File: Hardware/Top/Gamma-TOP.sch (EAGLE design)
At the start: 51 parts, among them SW6 SWITCH.MOM, SW7 SWITCH.MOM, U2 NRF52832_MODULE_MDBT42, U4 PCF8523

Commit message: Update to Top and Bottom Boards.  Top is not complete as of yet, and the bottom is ready for a check.  Routing not performed yet
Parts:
- removed R8, R9: 10k, LinnesLab-Passives:RESISTOR0603
- added C22: 100n, LinnesLab-Passives:CAPACITOR0603
- added C23, C24: 47p, LinnesLab-Passives:CAPACITOR0603
- added J1: (no value), LinnesLab-Connectors:CONN_07
- added JP2: (no value), LinnesLab-Switches:JUMPER-SMT_2_NO_SILK
- added LED5: RED, LinnesLab-LED:LED0603
- added LED6: YELLOW, LinnesLab-LED:LED0603
- added R1, R2: 0, LinnesLab-Passives:RESISTOR0603
- added R10, R16: 10k, LinnesLab-Passives:RESISTOR0603
- added R17, R18: 27, LinnesLab-Passives:RESISTOR0603
- added R19, R20: 1k, LinnesLab-Passives:RESISTOR0603
- added U5: FT231XS, LinnesLab-DigitalIC:FT231XS
- renumbered SW6 to SW1, SW7 to SW2
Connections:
- removed net BATT: R13.1, R14.2
- removed net CD1: SD2.CARD_DETECT
- removed net CHRG.STAT: CHRG2.STAT, R12.1
- removed net CS.OLED: U3./CS
- removed net DC.OLED: U3.DC/I2C_SA0
- removed net RESET.OLED: U3./RES
- removed net RXD: U2.P0.08
- removed net SD.CS: SD2.CS
- removed net SW1: SW1.1
- removed net SW2: SW2.1
- removed net TXD: U2.P0.06
- new net !CTS: JP2.2, U5.!CTS
- new net A4/BATT: R13.1, R14.2, U2.P0.28/AIN4
- new net A6/TIA: U2.P0.30/AIN6
- new net A7/PPG: U2.P0.31/AIN7
- new net D11/SW1: SW1.1, U2.P0.11
- new net D15/SW2: SW2.1, U2.P0.15
- new net D16/CS.OLED: U2.P0.16, U3./CS
- new net D27/CHRG.STATUS: CHRG2.STAT, R12.1, U2.P0.27
- new net D29/LED.CTRL: U2.P0.29/AIN5
- new net D3/RESET.OLED: U2.P0.03/AIN1, U3./RES
- new net D4/DC.OLED: U2.P0.04/AIN2, U3.DC/I2C_SA0
- new net D5/CD1: SD2.CARD_DETECT, U2.P0.05/AIN3
- new net D7/SD.CS: SD2.CS, U2.P0.07
- new net FT3V3: U5.3V3OUT
- new net N$23: R17.2, U5.USBDM
- new net N$24: R18.2, U5.USBDP
- new net N$25: LED5.C, R19.2
- new net N$26: LED6.C, R20.2
- new net RXD.FT: R2.1, U5.RXD
- new net RXD.NRF: R1.2, U2.P0.08
- new net RXLED: R19.1, U5.CBUS1
- new net TXD.FT: R1.1, U5.TXD
- new net TXD.NRF: R2.2, U2.P0.06
- new net TXLED: R20.1, U5.CBUS2
- net 3.3V: now also C22.2, LED5.A, LED6.A, R10.1, R16.1, U5.!RESET, U5.VCCIO; no longer R8.2, R9.2
- net DTR: now also U5.!DTR
- net GND: now also C22.1, C23.2, C24.1, JP2.1, U5.GND@16, U5.GND@6
- net SCL: now also R10.2; no longer R8.1
- net SDA: now also R16.2; no longer R9.1
- net USB+: now also C23.1, R18.1
- net USB-: now also C24.2, R17.1
- net V_USB: now also U5.VCC
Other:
- note added: "I don't remember if CTS needs to be grounded or left floating so here's a jumper to ground so it can be configued either way dynamically."
- note added: "TXD goes to RX on the other device RXD goes to TX on the other device"
- note added: "USB Serial"

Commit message: Finished Take 004 up until deletion of NFC capacitors.  Board partially routed
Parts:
- removed C22: 100n, LinnesLab-Passives:CAPACITOR0603
- removed C23, C24: 47p, LinnesLab-Passives:CAPACITOR0603
- removed CHRG2: MCP73831, LinnesLab-Power:MCP73831
- removed CORTEX1: CORTEX_DEBUG_PTH, LinnesLab-Connectors:CORTEX_DEBUG_PTH
- removed D4, D5: (no value), LinnesLab-DiscreteSemi:SCHOTTKY-USC
- removed JP2: (no value), LinnesLab-Switches:JUMPER-SMT_2_NO_SILK
- removed LDO2: MIC5504, LinnesLab-Power:MIC5504
- removed LED5: RED, LinnesLab-LED:LED0603
- removed LED6: YELLOW, LinnesLab-LED:LED0603
- removed R19, R20: 1k, LinnesLab-Passives:RESISTOR0603
- removed SD2: (no value), LinnesLab-Connectors:MICROSD
- removed U5: FT231XS, LinnesLab-DigitalIC:FT231XS
- removed USB2: USB.MICRO-BIGGERPADS, LinnesLab-Connectors:USB.MICRO-BIGGERPADS
- removed XTAL3: 32.7680kHz, LinnesLab-Clocks:CRYSTALECS-.327-12.5-12-C-TR
- added C1: 47p, LinnesLab-Passives:CAPACITOR0603
- added C3: 100n, LinnesLab-Passives:CAPACITOR0603
- added C4: 4.7u, LinnesLab-Passives:CAPACITOR0603
- added CHRG1: MCP73831, LinnesLab-Power:MCP73831
- added D2, D3: (no value), LinnesLab-DiscreteSemi:SCHOTTKY-USC
- added DEBUG1: CORTEX_DEBUG_PTH, LinnesLab-Connectors:CORTEX_DEBUG_PTH
- added JP1: (no value), LinnesLab-Switches:JUMPER-SMT_2_NO_SILK
- added LDO1: MIC5504, LinnesLab-Power:MIC5504
- added LED1: RED, LinnesLab-LED:LED0603
- added LED2: YELLOW, LinnesLab-LED:LED0603
- added R8: (no value), LinnesLab-Passives:RESISTOR0603
- added R9: 100k, LinnesLab-Passives:RESISTOR0603
- added SD1: (no value), LinnesLab-Connectors:MICROSD
- added U1: FT231XS, LinnesLab-DigitalIC:FT231XS
- added USB1: USB.MICRO-BIGGERPADS, LinnesLab-Connectors:USB.MICRO-BIGGERPADS
- added XTAL1: 32.768kHz, LinnesLab-Clocks:CRYSTALECS-.327-12.5-12-C-TR
- C10, C11: value 300p -> 2.2uF; device LinnesLab-Passives:CAPACITOR0603 -> LinnesLab-Passives:CAPACITOR0402
- C12: value 10u -> 1u; device LinnesLab-Passives:CAPACITOR0805 -> LinnesLab-Passives:CAPACITOR0603
- C13: value 2.2uF -> 4.7u; device LinnesLab-Passives:CAPACITOR0402 -> LinnesLab-Passives:CAPACITOR0603
- C14: value 100n -> 1u
- C15: value 2.2uF -> 10u; device LinnesLab-Passives:CAPACITOR0402 -> LinnesLab-Passives:CAPACITOR0805
- C16: value 10uF -> (none)
- C17: value 2.2uF -> (none); device LinnesLab-Passives:CAPACITOR0402 -> LinnesLab-Passives:CAPACITOR0603
- C18, C19: value 2.2uF -> 300p; device LinnesLab-Passives:CAPACITOR0402 -> LinnesLab-Passives:CAPACITOR0603
- C2: value 1u -> 47p
- C20: value 4.7u -> 100n
- C21: value 4.7u -> 1u
- C6: value 1u -> 10uF
- C7: value 1u -> 2.2uF; device LinnesLab-Passives:CAPACITOR0603 -> LinnesLab-Passives:CAPACITOR0402
- C8, C9: value (none) -> 2.2uF; device LinnesLab-Passives:CAPACITOR0603 -> LinnesLab-Passives:CAPACITOR0402
- J1: device LinnesLab-Connectors:CONN_07 -> LinnesLab-Connectors:CONN_07-1.27MM
- R1, R2: value 0 -> 27
- R10: value 10k -> 100k
- R11: value (none) -> 100k
- R12, R13: value 100k -> 0
- R14, R15: value 100k -> 10k
- R16, R5, R6: value 10k -> 1k
- R17: value 27 -> 1k
- R18: value 27 -> 10k
- R3: value 1k -> 100k
- R4: value 1k -> 10k
- U2: value NRF52832_MODULE_MDBT42 -> (none); device LinnesLab-Microcontrollers:NRF52832_MODULE_MDBT42 -> LinnesLab-Displays:DISP_OLED_UG-2864HSWEG01-NO-WRAPAROUND
- U3: value (none) -> NRF52832_MODULE_MDBT42; device LinnesLab-Displays:DISP_OLED_UG-2864HSWEG01-NO-WRAPAROUND -> LinnesLab-Microcontrollers:NRF52832_MODULE_MDBT42
- XTAL2: value 32.768kHz -> 32.7680kHz; FREQ (none) -> 32.7680KHZ
- renumbered L2 to L1
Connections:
- net !CTS: now also JP1.2, U1.!CTS; no longer JP2.2, U5.!CTS
- net 3.3V: now also C10.2, C11.2, C12.1, C15.2, C21.1, C3.2, D3.C, DEBUG1.VCC, J1.4, LDO1.OUT, LED1.A, LED2.A, R14.1, R15.1, R18.2, R9.2, SD1.VDD, U1.!RESET, U1.VCCIO, U2.VBAT; no longer C12.2, C17.2, C19.2, C2.1, C22.2, C6.1, CORTEX1.VCC, D1.C, LDO2.OUT, LED5.A, LED6.A, R10.1, R15.2, R16.1, R5.2, SD2.VDD, U3.VBAT, U5.!RESET, U5.VCCIO
- net A4/BATT: now also R10.1, R11.2, U3.P0.28/AIN4; no longer R13.1, R14.2, U2.P0.28/AIN4
- net A6/TIA: now also J1.6, U3.P0.30/AIN6; no longer U2.P0.30/AIN6
- net A7/PPG: now also J1.7, U3.P0.31/AIN7; no longer U2.P0.31/AIN7
- net CD2: now also SD1.CARD_DETECT1; no longer SD2.CARD_DETECT1
- net D11/SW1: now also U3.P0.11; no longer U2.P0.11
- net D15/SW2: now also U3.P0.15; no longer U2.P0.15
- net D16/CS.OLED: now also U2./CS, U3.P0.16; no longer U2.P0.16, U3./CS
- net D27/CHRG.STATUS: now also CHRG1.STAT, R3.1, U3.P0.27; no longer CHRG2.STAT, R12.1, U2.P0.27
- net D29/LED.CTRL: now also J1.5, U3.P0.29/AIN5; no longer U2.P0.29/AIN5
- net D3/RESET.OLED: now also U2./RES, U3.P0.03/AIN1; no longer U2.P0.03/AIN1, U3./RES
- net D4/DC.OLED: now also U2.DC/I2C_SA0, U3.P0.04/AIN2; no longer U2.P0.04/AIN2, U3.DC/I2C_SA0
- net D5/CD1: now also SD1.CARD_DETECT, U3.P0.05/AIN3; no longer SD2.CARD_DETECT, U2.P0.05/AIN3
- net D7/SD.CS: now also SD1.CS, U3.P0.07; no longer SD2.CS, U2.P0.07
- net DFU: now also SW4.B, U3.P0.20; no longer SW3.B, U2.P0.20
- net DTR: now also C20.1, U1.!DTR; no longer C14.1, U5.!DTR
- net FRST: now also U3.P0.22; no longer U2.P0.22
- net FT3V3: now also U1.3V3OUT; no longer U5.3V3OUT
- net GND: now also C1.1, C10.1, C11.1, C12.2, C13.2, C14.2, C15.1, C17.2, C18.2, C19.2, C21.2, C3.1, C4.1, C6.1, CHRG1.VSS, DEBUG1.GND@3, DEBUG1.GND@5, DEBUG1.GNDDTCT, DEBUG1.KEY, J1.3, JP1.1, LDO1.GND, R4.1, R8.1, R9.1, SD1.GND, SD1.GND1, SD1.VSS, SW3.B, SW4.A, U1.GND@16, U1.GND@6, U2.BS0, U2.BS2, U2.NC(GND)@1, U2.NC(GND)@2, U2.VLSS, U2.VSS, U3.GND@1, U3.GND@2, U3.GND@3, U3.GND@4, USB1.GND; no longer C10.2, C11.2, C12.1, C17.1, C18.1, C19.1, C20.2, C21.1, C22.1, C23.2, C24.1, C6.2, C7.2, C9.2, CHRG2.VSS, CORTEX1.GND@3, CORTEX1.GND@5, CORTEX1.GNDDTCT, CORTEX1.KEY, JP2.1, LDO2.GND, R14.1, R15.1, R6.1, SD2.GND, SD2.GND1, SD2.VSS, SW3.A, SW4.B, U2.GND@1, U2.GND@2, U2.GND@3, U2.GND@4, U3.BS0, U3.BS2, U3.NC(GND)@1, U3.NC(GND)@2, U3.VLSS, U3.VSS, U5.GND@16, U5.GND@6, USB2.GND
- net LED1: now also R16.2, U3.P0.17; no longer R3.2, U2.P0.17
- net LED2: now also R17.2, U3.P0.19; no longer R4.2, U2.P0.19
- net MISO: now also SD1.DATA_OUT, U3.P0.14; no longer SD2.DATA_OUT, U2.P0.14
- net MOSI: now also SD1.DATA_IN, U2.D1/SPI_SDIN/I2C_SDA, U3.P0.13; no longer SD2.DATA_IN, U2.P0.13, U3.D1/SPI_SDIN/I2C_SDA
- net N$1: now also R4.2, U2.BS1; no longer R6.2, U3.BS1
- net N$10: now also R17.1; no longer R4.1
- net N$11: now also U3.DCC; no longer U2.DCC
- net N$12: now also C14.1, U3.DEC4; no longer C7.1, U2.DEC4
- net N$13: now also C6.2, U2.VCC; no longer C16.2, U3.VCC
- net N$14: now also DEBUG1.NC/TDI; no longer CORTEX1.NC/TDI
- net N$15: now also C8.2, U2.VCOMH; no longer C18.2, U3.VCOMH
- net N$17: now also CHRG1.PROG, R8.2; no longer CHRG2.PROG, R11.2
- net N$19: now also XTAL2.1; no longer XTAL3.1
- net N$2: now also U2.IREF; no longer U3.IREF
- net N$20: now also XTAL2.2; no longer XTAL3.2
- net N$23: now also R1.2, U1.USBDM; no longer R17.2, U5.USBDM
- net N$24: now also R2.2, U1.USBDP; no longer R18.2, U5.USBDP
- net N$25: now also LED1.C, R5.2; no longer LED5.C, R19.2
- net N$26: now also LED2.C, R6.2; no longer LED6.C, R20.2
- net N$3: now also C9.2, U2.C2P; no longer C13.2, U3.C2P
- net N$4: now also C16.2, U3.P0.00/XL1, XTAL1.1; no longer C8.2, U2.P0.00/XL1, XTAL2.1
- net N$5: now also C9.1, U2.C2N; no longer C13.1, U3.C2N
- net N$6: now also C17.1, U3.P0.01/XL2, XTAL1.2; no longer C9.1, U2.P0.01/XL2, XTAL2.2
- net N$7: now also C7.2, U2.C1P; no longer C15.2, U3.C1P
- net N$8: now also C7.1, U2.C1N; no longer C15.1, U3.C1N
- net N$9: now also R16.1; no longer R3.1
- net P0.09/NFC1: now also C18.1, U3.P0.09; no longer C11.1, U2.P0.09
- net P0.10/NFC2: now also C19.1, U3.P0.10; no longer C10.1, U2.P0.10
- net RESET: now also C20.2, D3.A, DEBUG1.!RESET, R18.1, SW3.A, U3.P0.21/RESET; no longer C14.2, CORTEX1.!RESET, D1.A, R5.1, SW4.A, U2.P0.21/RESET
- net RXD.FT: now also R13.1, U1.RXD; no longer R2.1, U5.RXD
- net RXD.NRF: now also R12.2, U3.P0.08; no longer R1.2, U2.P0.08
- net RXLED: now also R5.1, U1.CBUS1; no longer R19.1, U5.CBUS1
- net SCK: now also SD1.SCLK, U2.D0/SPI_SCLK/I2C_SCK, U3.P0.12; no longer SD2.SCLK, U2.P0.12, U3.D0/SPI_SCLK/I2C_SCK
- net SCL: now also J1.2, R15.2, U3.P0.26; no longer R10.2, U2.P0.26
- net SDA: now also J1.1, R14.2, U3.P0.25; no longer R16.2, U2.P0.25
- net SWCLK: now also DEBUG1.SWDCLK/TCK, U3.SWDCLK; no longer CORTEX1.SWDCLK/TCK, U2.SWDCLK
- net SWDIO: now also DEBUG1.SWDIO/TMS, U3.SWDIO; no longer CORTEX1.SWDIO/TMS, U2.SWDIO
- net SWO: now also DEBUG1.SWO/TDO, U3.P0.18/SWO; no longer CORTEX1.SWO/TDO, U2.P0.18/SWO
- net TXD.FT: now also R12.1, U1.TXD; no longer R1.1, U5.TXD
- net TXD.NRF: now also R13.2, U3.P0.06; no longer R2.2, U2.P0.06
- net TXLED: now also R6.1, U1.CBUS2; no longer R20.1, U5.CBUS2
- net USB+: now also C2.1, R2.1, USB1.D+; no longer C23.1, R18.1, USB2.D+
- net USB-: now also C1.2, R1.1, USB1.D-; no longer C24.2, R17.1, USB2.D-
- net VIN: now also C4.2, CHRG1.VIN, D1.C, D2.C, LDO1.EN, LDO1.IN, R3.2; no longer C21.2, CHRG2.VIN, D4.C, D5.C, LDO2.EN, LDO2.IN, R12.2
- net VLIPO: now also C13.1, CHRG1.VBAT, D1.A, R10.2; no longer C20.1, CHRG2.VBAT, D4.A, R13.2
- net V_USB: now also D2.A, U1.VCC, USB1.V+; no longer D5.A, U5.VCC, USB2.V+
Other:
- note added: "Gamma Top Version A"
- note added: "Pins"
- moved on the sheet: C10, C11, C12, C13, C14, C15, C16, C17, C18, C19, C2, C20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

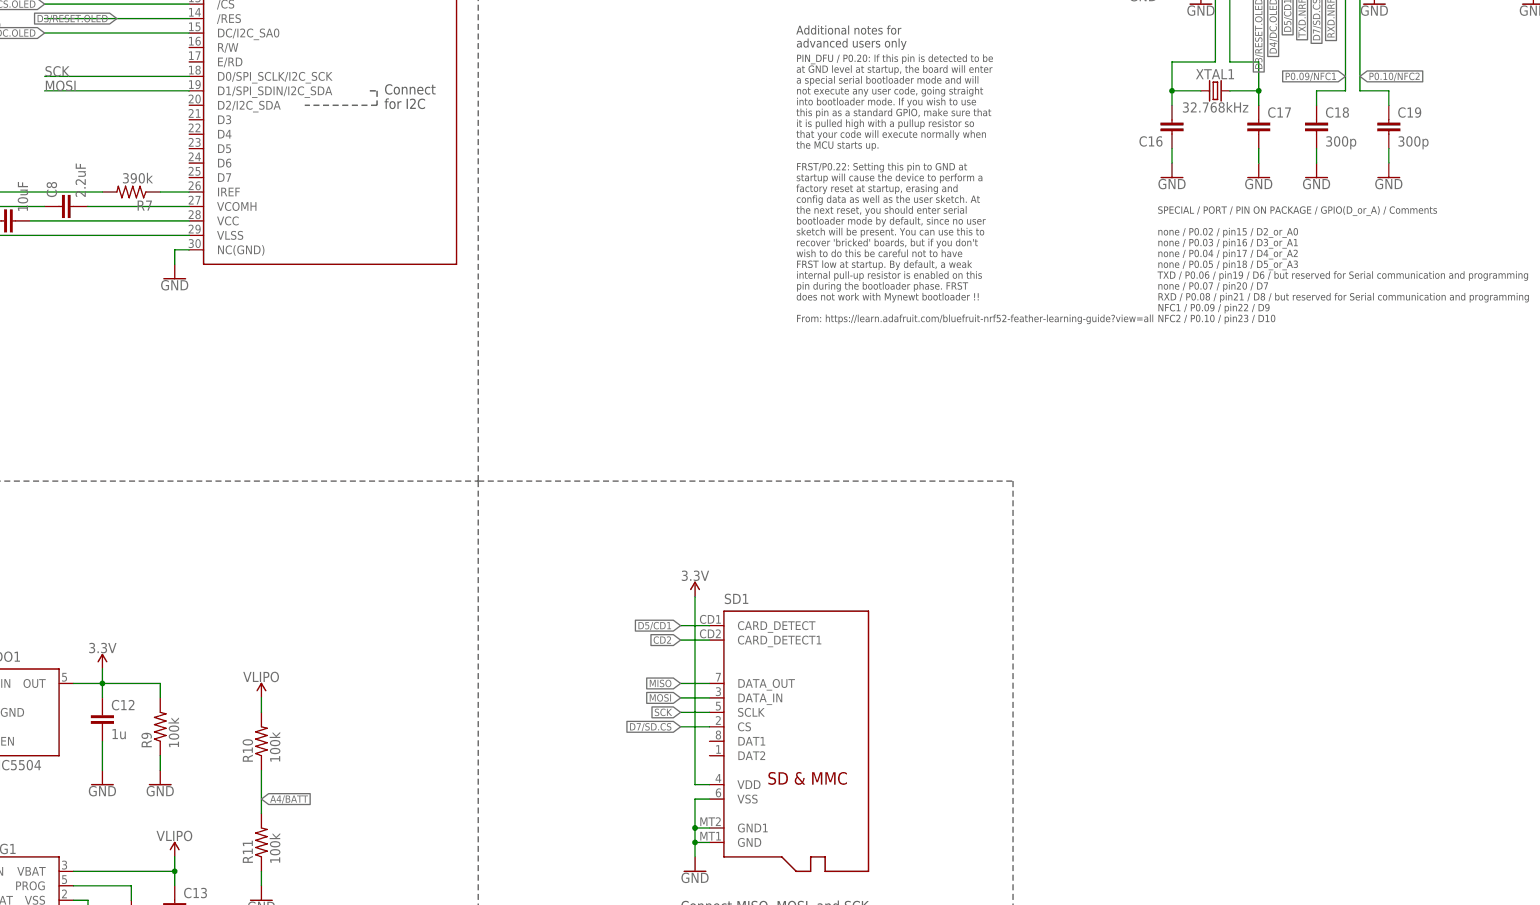
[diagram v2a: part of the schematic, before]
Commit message: This is the routing as of Take 006 before the removal of the SD Card
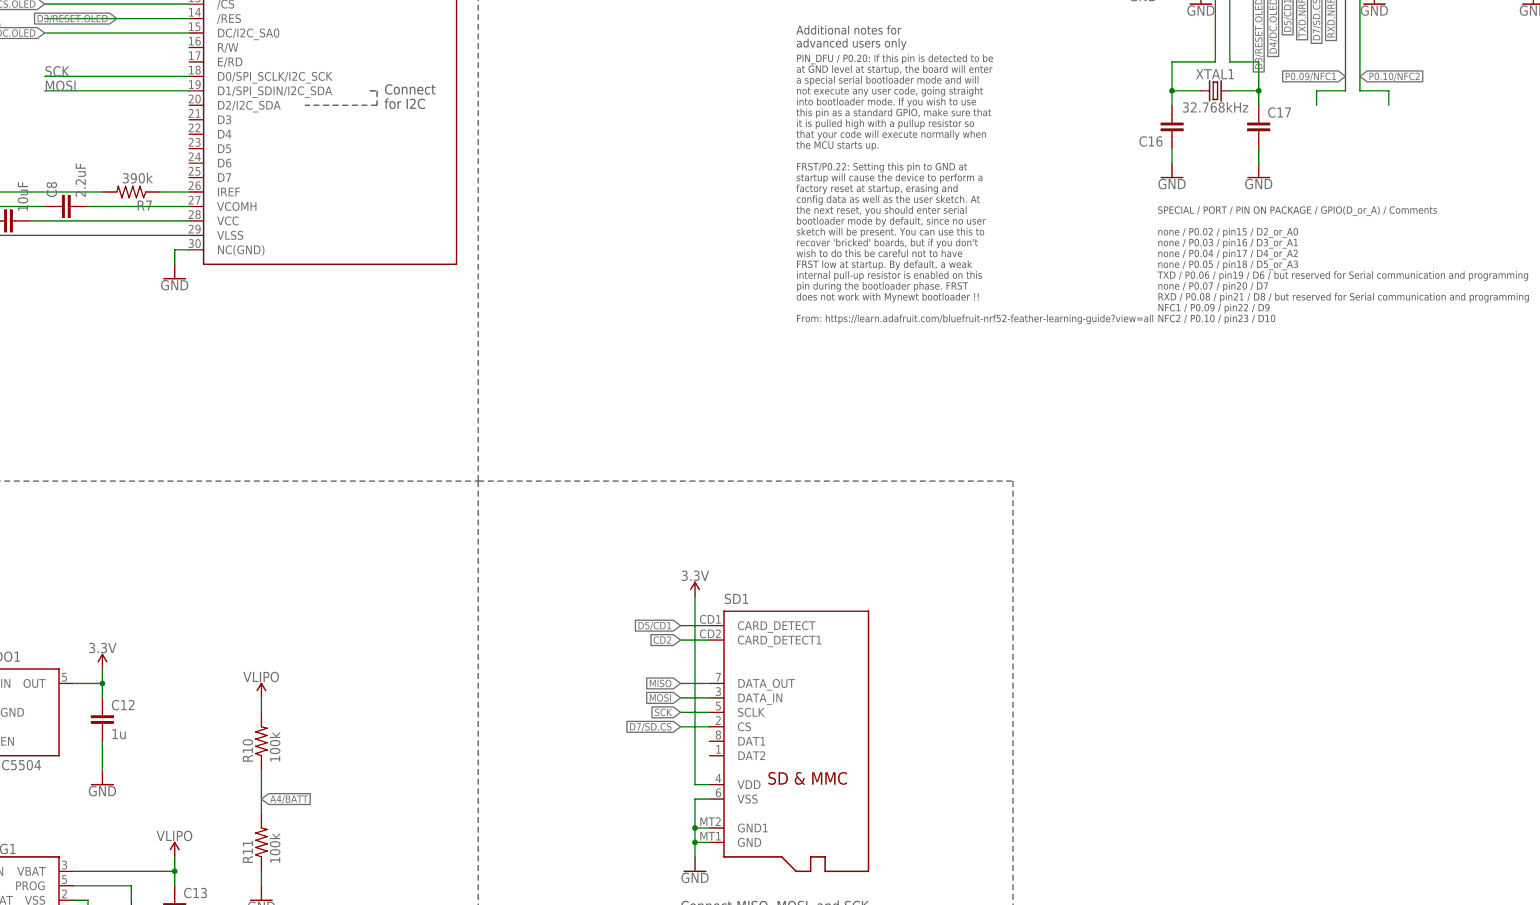
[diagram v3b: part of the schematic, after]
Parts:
- removed C18, C19: 300p, LinnesLab-Passives:CAPACITOR0603
- removed R9: 100k, LinnesLab-Passives:RESISTOR0603
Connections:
- net 3.3V: no longer R9.2
- net GND: no longer C18.2, C19.2, R9.1
- net P0.09/NFC1: no longer C18.1
- net P0.10/NFC2: no longer C19.1
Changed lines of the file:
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@@
 <part name="GND15" library="LinnesLab-Symbols" deviceset="GND" device=""/>
 <part name="GND16" library="LinnesLab-Symbols" deviceset="GND" device=""/>
-<part name="GND17" library="LinnesLab-Symbols" deviceset="GND" device=""/>
-<part name="GND18" library="LinnesLab-Symbols" deviceset="GND" device=""/>
 <part name="GND19" library="LinnesLab-Symbols" deviceset="GND" device=""/>
 <part name="GND20" library="LinnesLab-Symbols" deviceset="GND" device=""/>
@@
 <part name="C16" library="LinnesLab-Passives" deviceset="CAPACITOR" device="0603" package3d_urn="urn:adsk.eagle:package:15661989/2"/>
 <part name="C17" library="LinnesLab-Passives" deviceset="CAPACITOR" device="0603" package3d_urn="urn:adsk.eagle:package:15661989/2"/>
-<part name="C19" library="LinnesLab-Passives" deviceset="CAPACITOR" device="0603" package3d_urn="urn:adsk.eagle:package:15661989/2" value="300p"/>
-<part name="C18" library="LinnesLab-Passives" deviceset="CAPACITOR" device="0603" package3d_urn="urn:adsk.eagle:package:15661989/2" value="300p"/>
 <part name="C15" library="LinnesLab-Passives" deviceset="CAPACITOR" device="0805" package3d_urn="urn:adsk.eagle:package:15662010/2" value="10u"/>
 <part name="L1" library="LinnesLab-Passives" deviceset="INDUCTOR" device="0603" override_package3d_urn="urn:adsk.eagle:package:18592195/2" override_package_urn="urn:adsk.eagle:footprint:18592196/1" value="10u"/>
@@
 <part name="SUPPLY16" library="LinnesLab-Symbols" deviceset="VLIPO" device=""/>
 <part name="GND43" library="LinnesLab-Symbols" deviceset="GND" device=""/>
-<part name="R9" library="LinnesLab-Passives" deviceset="RESISTOR" device="0603" package3d_urn="urn:adsk.eagle:package:15661944/2" value="100k"/>
-<part name="GND44" library="LinnesLab-Symbols" deviceset="GND" device=""/>
 <part name="SUPPLY17" library="LinnesLab-Symbols" deviceset="VIN" device=""/>
 <part name="GND4" library="LinnesLab-Symbols" deviceset="GND" device=""/>
@@
 <attribute name="VALUE" x="106.68" y="60.706" size="1.778" layer="96" align="top-center"/>
 </instance>
-<instance part="GND17" gate="G$1" x="109.22" y="30.48" smashed="yes">
-<attribute name="VALUE" x="109.22" y="30.226" size="1.778" layer="96" align="top-center"/>
-</instance>
-<instance part="GND18" gate="G$1" x="96.52" y="30.48" smashed="yes">
-<attribute name="VALUE" x="96.52" y="30.226" size="1.778" layer="96" align="top-center"/>
-</instance>
 <instance part="GND19" gate="G$1" x="86.36" y="30.48" smashed="yes">
 <attribute name="VALUE" x="86.36" y="30.226" size="1.778" layer="96" align="top-center"/>
@@
 <attribute name="VALUE" x="87.884" y="35.941" size="1.778" layer="96"/>
 </instance>
-<instance part="C19" gate="G$1" x="109.22" y="38.1" smashed="yes">
-<attribute name="NAME" x="110.744" y="41.021" size="1.778" layer="95"/>
-<attribute name="VALUE" x="110.744" y="35.941" size="1.778" layer="96"/>
-</instance>
-<instance part="C18" gate="G$1" x="96.52" y="38.1" smashed="yes">
-<attribute name="NAME" x="98.044" y="41.021" size="1.778" layer="95"/>
-<attribute name="VALUE" x="98.044" y="35.941" size="1.778" layer="96"/>
-</instance>
 <instance part="C15" gate="G$1" x="66.04" y="73.66" smashed="yes" rot="R180">
 <attribute name="NAME" x="64.516" y="70.739" size="1.778" layer="95" rot="R180"/>
@@
 <instance part="GND43" gate="G$1" x="-119.38" y="-101.6" smashed="yes">
 <attribute name="VALUE" x="-119.38" y="-101.854" size="1.778" layer="96" align="top-center"/>
-</instance>
-<instance part="R9" gate="G$1" x="-106.68" y="-66.04" smashed="yes" rot="R90">
-<attribute name="NAME" x="-108.1786" y="-69.85" size="1.778" layer="95" rot="R90"/>
-<attribute name="VALUE" x="-103.378" y="-69.85" size="1.778" layer="96" rot="R90"/>
-</instance>
-<instance part="GND44" gate="G$1" x="-106.68" y="-76.2" smashed="yes">
-<attribute name="VALUE" x="-106.68" y="-76.454" size="1.778" layer="96" align="top-center"/>
 </instance>
 <instance part="SUPPLY17" gate="G$1" x="-165.1" y="-55.88" smashed="yes">
@@
 <pinref part="GND20" gate="G$1" pin="GND"/>
 <pinref part="C16" gate="G$1" pin="1"/>
-</segment>
-<segment>
-<pinref part="C18" gate="G$1" pin="2"/>
-<pinref part="GND18" gate="G$1" pin="GND"/>
-<wire x1="96.52" y1="33.02" x2="96.52" y2="35.56" width="0.1524" layer="91"/>
-</segment>
-<segment>
-<pinref part="C19" gate="G$1" pin="2"/>
-<pinref part="GND17" gate="G$1" pin="GND"/>
-<wire x1="109.22" y1="33.02" x2="109.22" y2="35.56" width="0.1524" layer="91"/>
 </segment>
 <segment>
@@
 </segment>
 <segment>
-<pinref part="R9" gate="G$1" pin="1"/>
-<pinref part="GND44" gate="G$1" pin="GND"/>
-<wire x1="-106.68" y1="-73.66" x2="-106.68" y2="-71.12" width="0.1524" layer="91"/>
-</segment>
-<segment>
 <wire x1="281.94" y1="-78.74" x2="279.4" y2="-78.74" width="0.1524" layer="91"/>
 <wire x1="279.4" y1="-81.28" x2="279.4" y2="-78.74" width="0.1524" layer="91"/>
@@
 <wire x1="-116.84" y1="-55.88" x2="-116.84" y2="-58.42" width="0.1524" layer="91"/>
 <junction x="-116.84" y="-58.42"/>
-<wire x1="-116.84" y1="-58.42" x2="-106.68" y2="-58.42" width="0.1524" layer="91"/>
-<pinref part="R9" gate="G$1" pin="2"/>
-<wire x1="-106.68" y1="-58.42" x2="-106.68" y2="-60.96" width="0.1524" layer="91"/>
 </segment>
 <segment>
@@
 <wire x1="96.52" y1="45.72" x2="101.6" y2="45.72" width="0.1524" layer="91"/>
 <wire x1="96.52" y1="45.72" x2="96.52" y2="43.18" width="0.1524" layer="91"/>
-<pinref part="C18" gate="G$1" pin="1"/>
 <pinref part="U3" gate="G$1" pin="P0.09"/>
 <label x="101.6" y="48.26" size="1.27" layer="95" rot="R180" xref="yes"/>
@@
 <wire x1="104.14" y1="45.72" x2="109.22" y2="45.72" width="0.1524" layer="91"/>
 <wire x1="109.22" y1="45.72" x2="109.22" y2="43.18" width="0.1524" layer="91"/>
-<pinref part="C19" gate="G$1" pin="1"/>
 <pinref part="U3" gate="G$1" pin="P0.10"/>
 <label x="104.14" y="48.26" size="1.27" layer="95" xref="yes"/>

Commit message: Partway through Take 007
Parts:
- removed C21: 1u, LinnesLab-Passives:CAPACITOR0603
- removed SD1: (no value), LinnesLab-Connectors:MICROSD
- removed U4: PCF8523, LinnesLab-Clocks:PCF8523
- removed XTAL2: 32.7680kHz, LinnesLab-Clocks:CRYSTALECS-.327-12.5-12-C-TR
- C8: device LinnesLab-Passives:CAPACITOR0402 -> LinnesLab-Passives:CAPACITOR0603
- LED2: value YELLOW -> BLUE
- LED4: value BLUE -> YELLOW
- renumbered XTAL1 to Y1
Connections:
- removed net CD2: SD1.CARD_DETECT1
- removed net N$19: U4.OSCO, XTAL2.1
- removed net N$20: U4.OSCI, XTAL2.2
- removed net VBATT: U4.VBAT
- net 3.3V: now also LED3.A, LED4.A; no longer C21.1, LED1.A, LED2.A, SD1.VDD, U4.VDD
- net D5/CD1: no longer SD1.CARD_DETECT
- net D7/SD.CS: no longer SD1.CS
- net GND: now also LED1.C, LED2.C; no longer C21.2, LED3.C, LED4.C, SD1.GND, SD1.GND1, SD1.VSS, U4.VSS
- net MISO: no longer SD1.DATA_OUT
- net MOSI: no longer SD1.DATA_IN
- net N$10: now also LED2.A; no longer LED4.A
- net N$25: now also LED3.C; no longer LED1.C
- net N$26: now also LED4.C; no longer LED2.C
- net N$9: now also LED1.A; no longer LED3.A
- net SCK: no longer SD1.SCLK
- net SCL: no longer U4.SCL
- net SDA: no longer U4.SDA
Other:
- note added: "Reset Circuit"
- note removed: "Back-up battery if desired"
- note removed: "Connect MISO, MOSI, and SCK to appropriate pins on microcontroller. Those are SPI pins and are generally prespecified. You have more flexibility with the SD.CS pin."
- note removed: "I2C Address = 0x68h"
- note removed: "RTC"
- note removed: "Real-Time Clock"
- note removed: "SD Module"
- moved on the sheet: LED1, LED2, LED3, LED4
